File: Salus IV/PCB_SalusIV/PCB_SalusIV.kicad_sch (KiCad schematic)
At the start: 14 parts, among them J1 DC-005-5A-2.0, J2 DC-005-5A-2.0, Q1 IRFR5305TRPBF, Q2 IRFR5305TRPBF, Q3 IRFR5305TRPBF, Q4 IRFR5305TRPBF

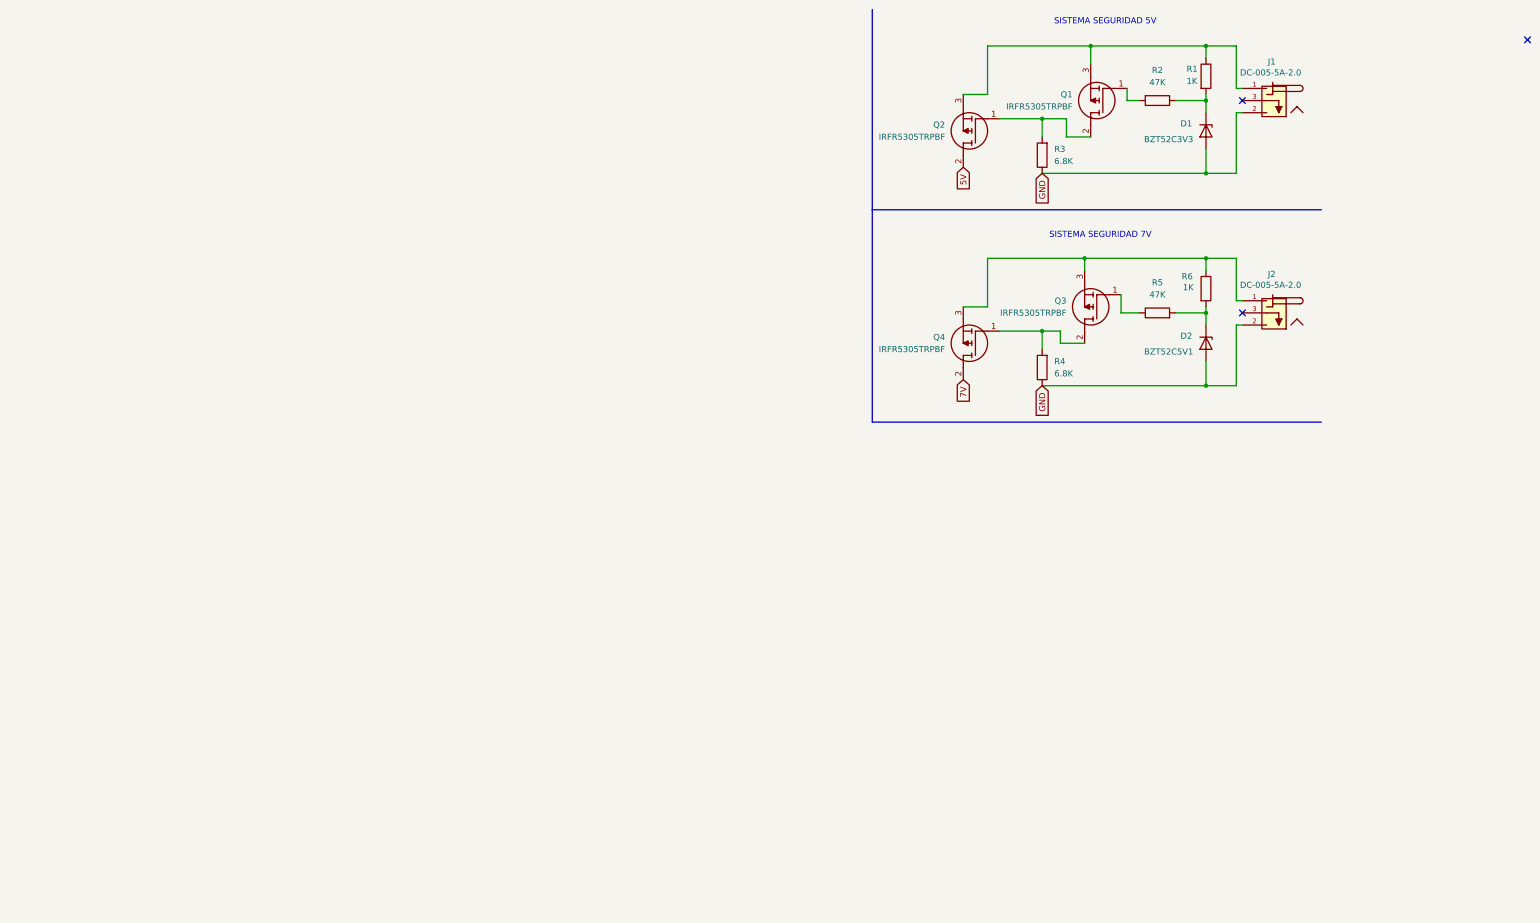
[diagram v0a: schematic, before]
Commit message: se agrego logica de Rasp y algunos conectores
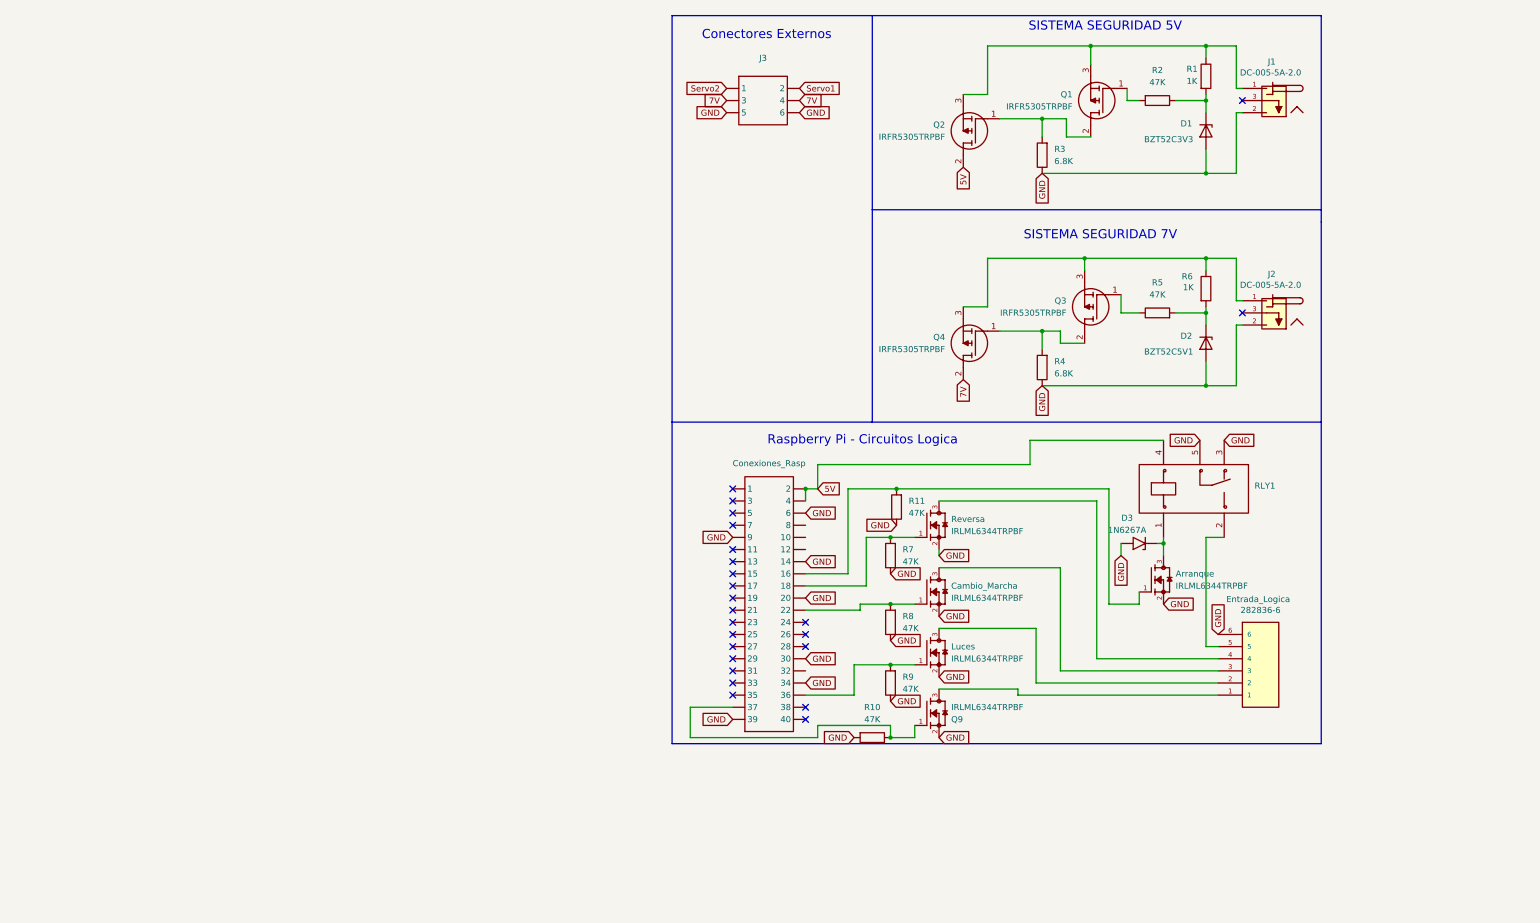
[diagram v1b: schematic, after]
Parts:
- added Arranque, Cambio_Marcha, Luces, Q9, Reversa: IRLML6344TRPBF, Footprints:TRANS_IRLML6344TRPBF, symbol Simbolos:IRLML6344TRPBF
- added Conexiones_Rasp: ~, Footprints:IDC-TH_40P-P2.54_C9138, symbol Simbolos:HDR-IDC-2.54-2X20P
- added D3: 1N6267A, Diode_THT:D_DO-201AE_P15.24mm_Horizontal, symbol Diode:1N62xxA
- added Entrada_Logica: 282836-6, 282836-6:TE_282836-6, symbol Simbolos:282836-6
- added J3: ~, Footprints:HDR-TH_6P-P2.54-V-M-R2-C3-S2.54-1, symbol Simbolos:Header-Male-2.54_2x3
- added R10, R11, R7, R8, R9: 47K, Resistor_SMD:R_1206_3216Metric, symbol Device:R
- added RLY1: ~, ProLib_pcs_2026-02-12 (1):RELAY-TH_SRD-XXVDC-XL-C, symbol Simbolos:SRD-05VDC-SL-C
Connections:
- net 5V: now also Conexiones_Rasp.2, Conexiones_Rasp.4, RLY1.4
- net 7V: now also J3.3, J3.4
- net GND: now also Arranque.2, Cambio_Marcha.2, Conexiones_Rasp.14, Conexiones_Rasp.20, Conexiones_Rasp.30, Conexiones_Rasp.34, Conexiones_Rasp.39, Conexiones_Rasp.6, Conexiones_Rasp.9, D3.2 (A2), Entrada_Logica.6, J3.5, J3.6, Luces.2, Q9.2, R10.2, R11.1, R7.1, R8.1, R9.1, RLY1.3, RLY1.5, Reversa.2
- new net: Conexiones_Rasp.37, Q9.1, R10.1
- new net: Entrada_Logica.1, Q9.3
- new net: Arranque.1, Conexiones_Rasp.16, R11.2
- new net: Arranque.3, D3.1 (A1), RLY1.1
- new net: Entrada_Logica.5, RLY1.2
- new net: Conexiones_Rasp.18, R7.2, Reversa.1
- new net: Entrada_Logica.4, Reversa.3
- new net: Conexiones_Rasp.36, Luces.1, R9.2
- new net: Entrada_Logica.2, Luces.3
- new net: Cambio_Marcha.3, Entrada_Logica.3
- new net: Cambio_Marcha.1, Conexiones_Rasp.22, R8.2
- new net Servo1: J3.2
- new net Servo2: J3.1
- no-connect marks 3 -> 24
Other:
- note added: "Conectores Externos"
- note added: "Raspberry Pi - Circuitos Logica"
- company: (none) -> A-EYE
- title: (none) -> PCB Salus IV

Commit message: pusheo por seguridad, avanzado Esquematico
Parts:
- added Arranque1: IRLML6344TRPBF, Footprints:TRANS_IRLML6344TRPBF, symbol Simbolos:IRLML6344TRPBF
- added C1: 100nF, Capacitor_SMD:C_0402_1005Metric, symbol Device:C
- added D4: LED_Encendido, LED_SMD:LED_0603_1608Metric, symbol Device:LED
- added D5: 1N6267A, Diode_THT:D_DO-201AE_P15.24mm_Horizontal, symbol Diode:1N62xxA
- added JP1, JP10, JP11, JP12, JP13, JP14, JP15, JP16, JP17, JP18, JP2, JP3, JP4, JP5, JP6, JP7, JP8, JP9: Jumper_Soldado, Jumper:SolderJumper-2_P1.3mm_Open_Pad1.0x1.5mm, symbol Jumper:SolderJumper_2_Open
- added P1, P2: ~, Footprints:HDR-TH_16P-P2.54-V-M-R2-C8-S2.54, symbol Simbolos:Header-Male-2.54_2x8
- added P3: ~, Footprints:CONN-TH_2P-P5.00_CPC3703CTR, symbol Simbolos:WJ127-5.0-2P
- added R12, R16, R17, R18, R19, R20, R21, R22, R23, R24, R25, R26, R27, R28, R29, R30, R31, R32, R33, R34: 4.7K, Resistor_SMD:R_1206_3216Metric, symbol Device:R
- added R13: 4.7K, symbol Device:R
- added R14: 10K, Resistor_SMD:R_1206_3216Metric, symbol Device:R
- added R15: 390, Resistor_SMD:R_1206_3216Metric, symbol Device:R
- added R35: 47K, Footprints:RES-TH_BD2.5-L6.5-P10.50-D0.6, symbol Device:R
- added R36: 1.5K, Footprints:RES-TH_BD1.9-L3.3-P7.30-D0.5, symbol Device:R
- added R37: 47K, Resistor_SMD:R_1206_3216Metric, symbol Device:R
- added RLY2: ~, ProLib_pcs_2026-02-12 (1):RELAY-TH_SRD-XXVDC-XL-C, symbol Simbolos:SRD-05VDC-SL-C
- added U1: ~, Footprints:SSOP-28_L10.2-W5.3-P0.65-LS7.8-BL, symbol Simbolos:MCP23017T-E/SS
- added U2: ~, ProLib_pcs_2026-02-13 (2):VQFN-24_L4.0-W4.0-P0.50-BL-EP2.5, symbol Simbolos:TCA9548ARGER
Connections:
- net GND: now also Arranque1.2, C1.2, D4.1 (K), D5.2 (A2), P3.2, R36.2, R37.1, U1.10 (VSS), U1.15 (A0), U1.16 (A1), U1.17 (A2), U2.18 (A2), U2.22 (A0), U2.23 (A1), U2.25 (EP), U2.9 (GND)
- net 5V renamed +5V
- net +5V: now also R15.1, RLY2.4
- new net: JP16.2 (B), R18.1
- new net: R35.1, RLY2.2
- new net: JP13.2 (B), R21.1
- new net: JP3.2 (B), R31.1
- new net: JP9.2 (B), R25.1
- new net: JP12.2 (B), R22.1
- new net: JP18.2 (B), R16.1
- new net: JP11.2 (B), R23.1
- new net: JP5.2 (B), R29.1
- new net: JP2.2 (B), R32.1
- new net: JP1.2 (B), R33.1
- new net: JP7.2 (B), R27.1
- new net: JP17.2 (B), R17.1
- new net: JP4.2 (B), R30.1
- new net: JP6.2 (B), R28.1
- new net: D4.2 (A), R15.2
- new net: Arranque1.3, D5.1 (A1), RLY2.1
- new net: JP14.2 (B), R20.1
- new net: JP8.2 (B), R26.1
- new net: R14.1, U1.18 (RESET#)
- new net: JP15.2 (B), R19.1
- new net: JP10.2 (B), R24.1
- new net +3.3V: C1.1, JP1.1 (A), JP10.1 (A), JP11.1 (A), JP12.1 (A), JP13.1 (A), JP14.1 (A), JP15.1 (A), JP16.1 (A), JP17.1 (A), JP18.1 (A), JP2.1 (A), JP3.1 (A), JP4.1 (A), JP5.1 (A), JP6.1 (A), JP7.1 (A), JP8.1 (A), JP9.1 (A), R12.1, R13.1, R14.2, R34.1, U1.9 (VDD), U2.21 (VCC)
- new net 60V: P3.1, RLY2.5
- new net ADC_ES: R35.2, R36.1
- new net Control_Bat: Arranque1.1, R37.2
- new net Expansor 1: P1.1, U1.21 (GPA0)
- new net Expansor 10: P1.4, U1.7 (GPB6)
- new net Expansor 11: P1.6, U1.6 (GPB5)
- new net Expansor 12: P1.8, U1.5 (GPB4)
- new net Expansor 13: P1.10, U1.4 (GPB3)
- new net Expansor 14: P1.12, U1.3 (GPB2)
- new net Expansor 15: P1.14, U1.2 (GPB1)
- new net Expansor 16: P1.16, U1.1 (GPB0)
- new net Expansor 2: P1.3, U1.22 (GPA1)
- new net Expansor 3: P1.5, U1.23 (GPA2)
- new net Expansor 4: P1.7, U1.24 (GPA3)
- new net Expansor 5 : P1.9, U1.25 (GPA4)
- new net Expansor 6 : P1.11, U1.26 (GPA5)
- new net Expansor 7 : P1.13, U1.27 (GPA6)
- new net Expansor 8: P1.15, U1.28 (GPA7)
- new net Expansor 9: P1.2, U1.8 (GPB7)
- new net RESET: R34.2, U2.24 (RESET#)
- new net SC0: P2.4, R17.2, U2.2 (SC0)
- new net SC1: P2.8, R19.2, U2.4 (SC1)
- new net SC2: P2.12, R21.2, U2.6 (SC2)
- new net SC3: P2.16, R23.2, U2.8 (SC3)
- new net SC4: P2.3, R25.2, U2.11 (SC4)
- new net SC5: P2.7, R27.2, U2.13 (SC5)
- new net SC6: P2.11, R33.2, U2.15 (SC6)
- new net SC7: P2.15, R31.2, U2.17 (SC7)
- new net SCL: R29.2, U2.19 (SCL)
- new net SCL_Expansor: R12.2, U1.12 (SCK)
- new net SD0: P2.2, R16.2, U2.1 (SD0)
- new net SD1: P2.6, R18.2, U2.3 (SD1)
- new net SD2: P2.10, R20.2, U2.5 (SD2)
- new net SD3: P2.14, R22.2, U2.7 (SD3)
- new net SD4: P2.1, R24.2, U2.10 (SD4)
- new net SD5: P2.5, R26.2, U2.12 (SD5)
- new net SD6: P2.9, R32.2, U2.14 (SD6)
- new net SD7: P2.13, R30.2, U2.16 (SD7)
- new net SDA: R28.2, U2.20 (SDA)
- new net SDA_Expansor: R13.2, U1.13 (SDA)
- no-connect marks 24 -> 29
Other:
- note added: "ESP32"
- note added: "Extensor Gpios"
- note added: "LED Encendido"
- note added: "Medidor de Bateria"
- note added: "Multiplexor I2C"

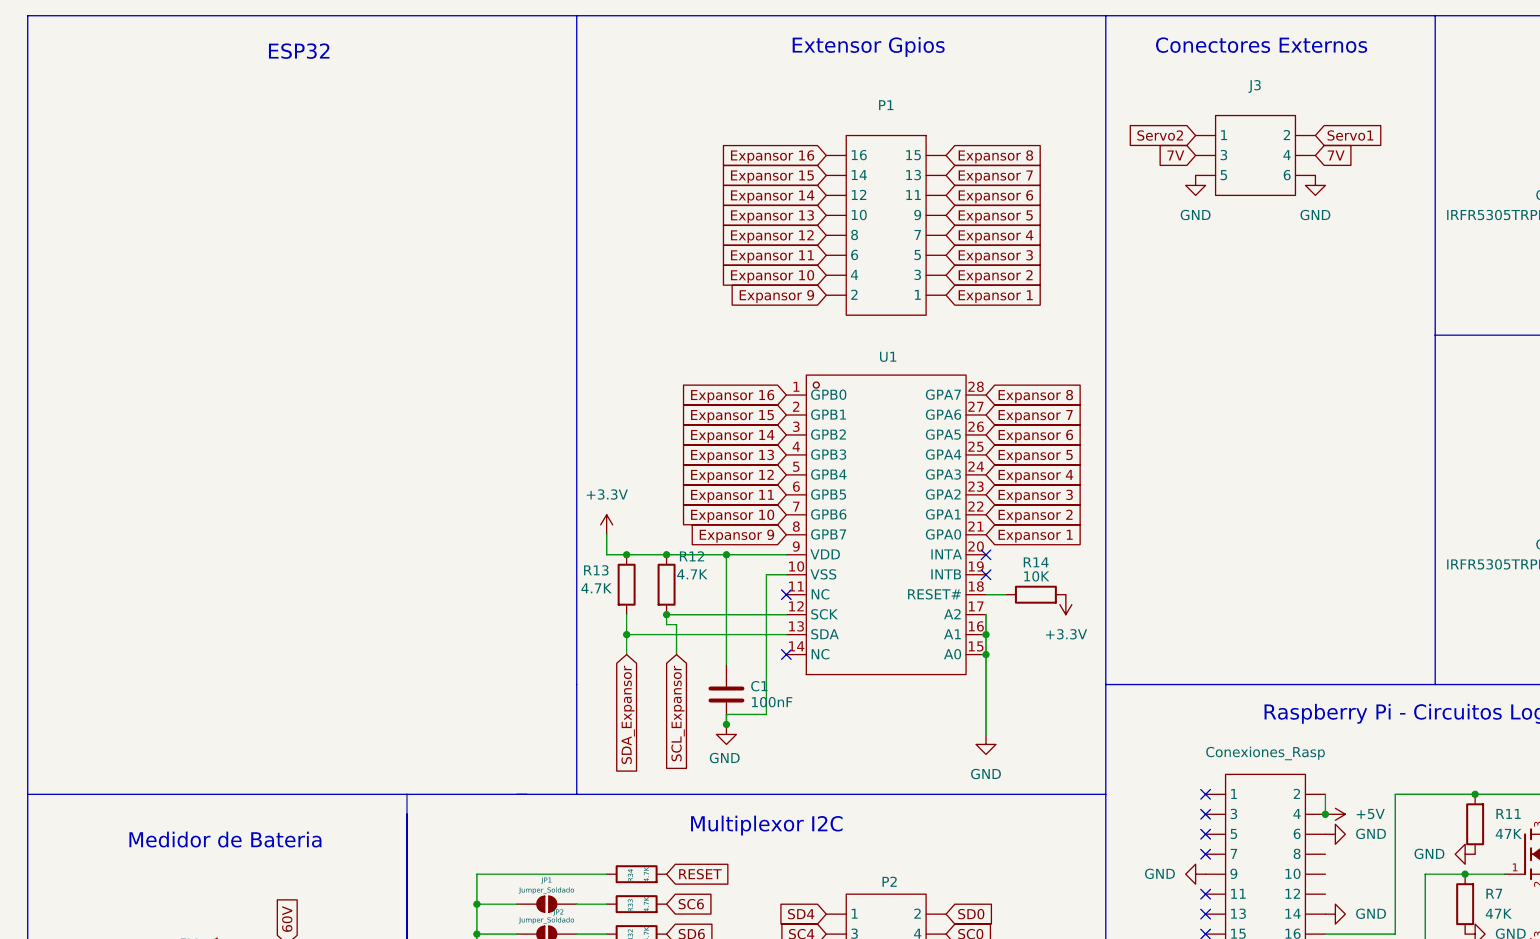
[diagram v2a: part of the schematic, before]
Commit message: Agregamos Huellas y se dividio en hojas jerarquicas
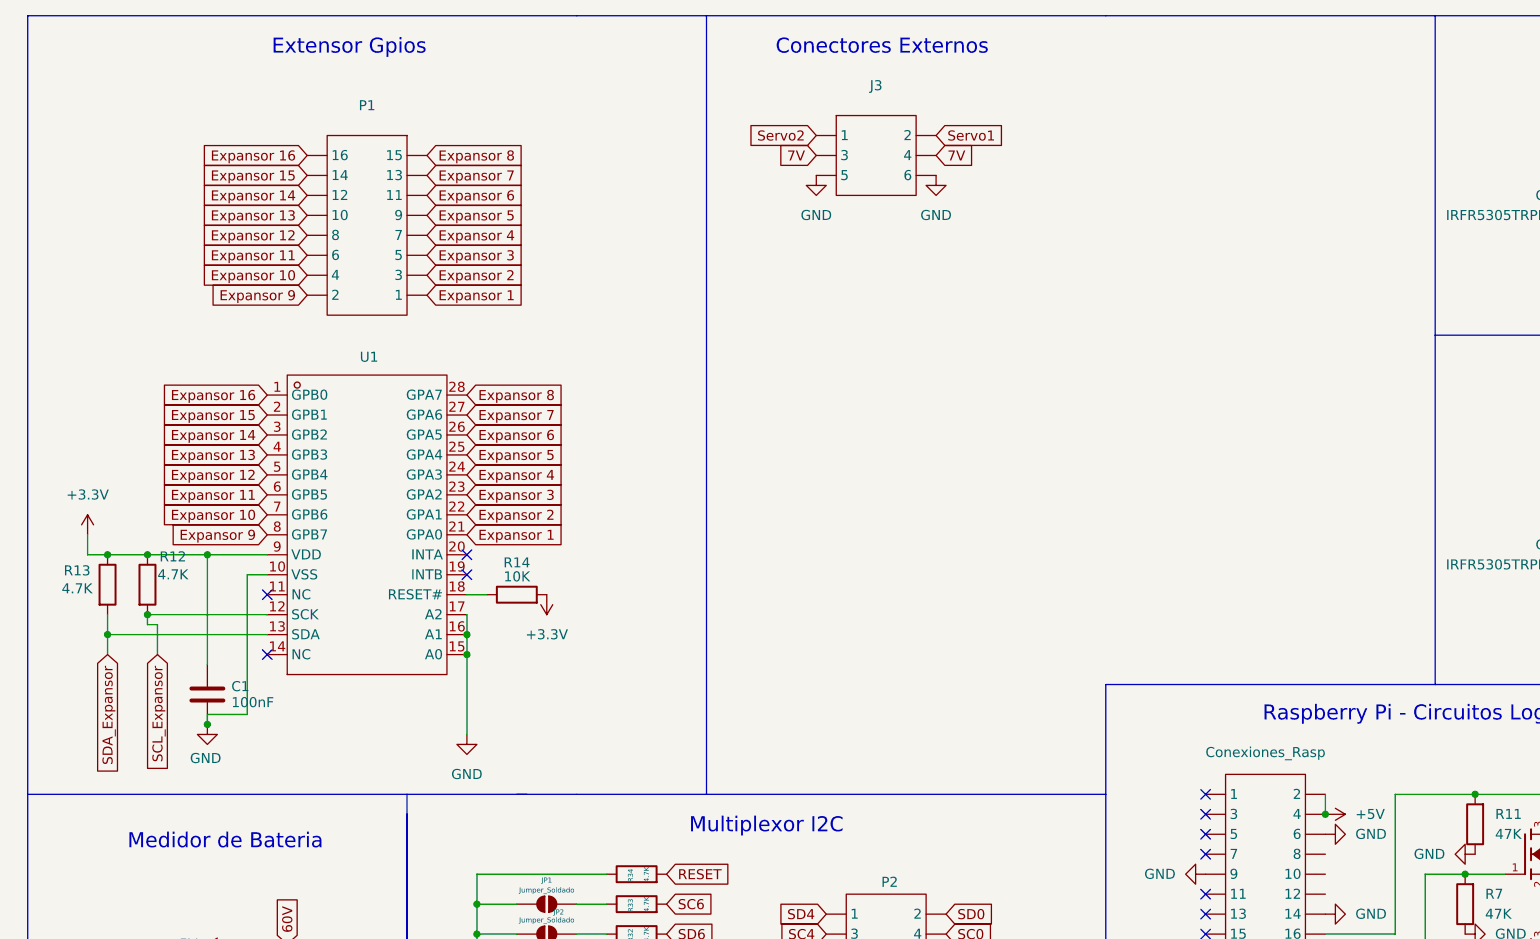
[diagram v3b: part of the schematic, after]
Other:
- note removed: "ESP32"
- moved on the sheet: C1, J3, P1, R12, R13, R14, U1
